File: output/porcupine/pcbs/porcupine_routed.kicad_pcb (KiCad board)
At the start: 2 copper layers, 129.4 x 113.9 mm, 54 parts, among them J1 Jumper, J2 Jumper

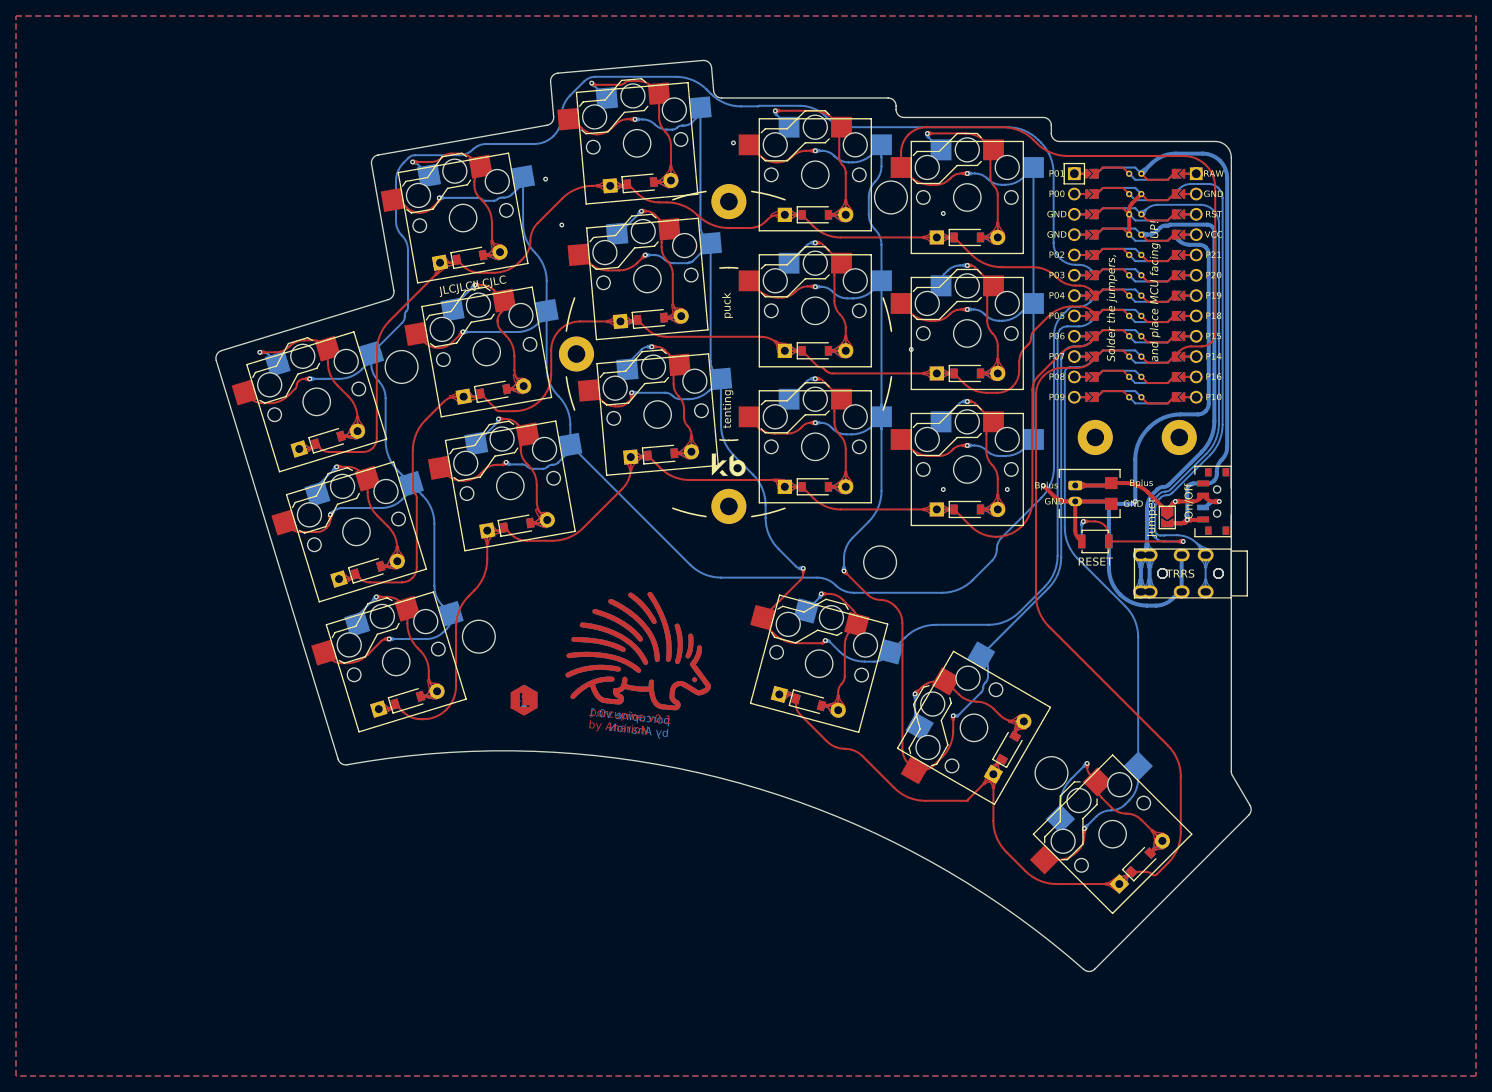
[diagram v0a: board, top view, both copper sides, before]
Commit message: Add new logo
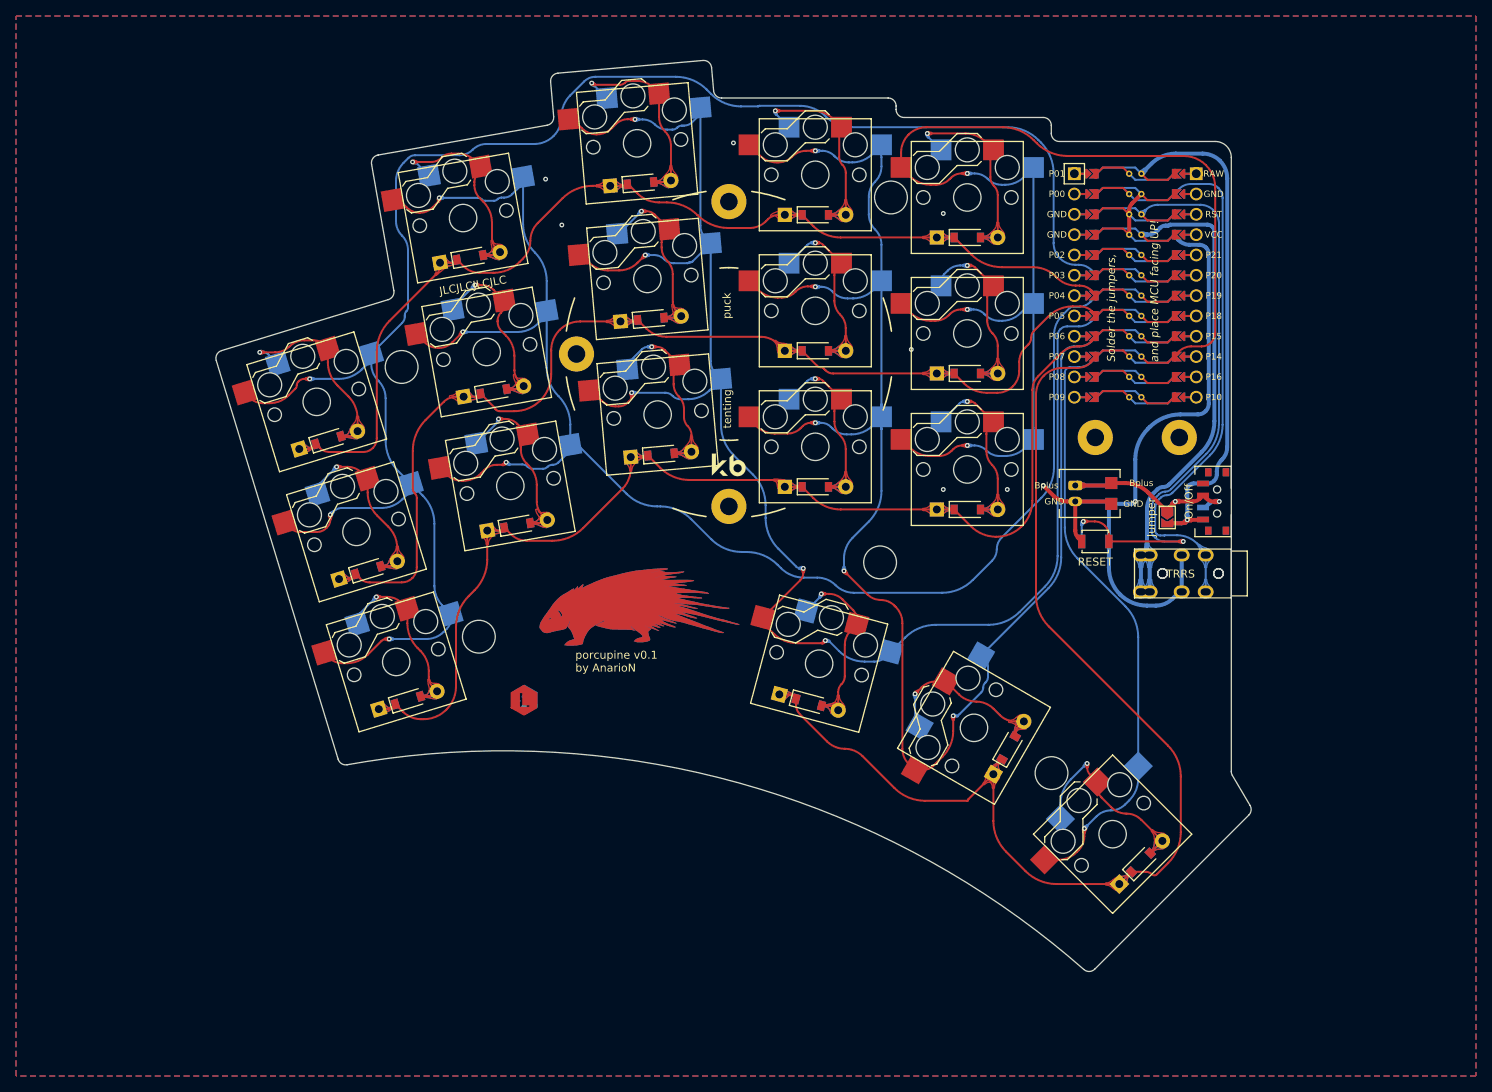
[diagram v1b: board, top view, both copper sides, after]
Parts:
- moved LOGO_B 5.28 mm to (205.4, 143.9), turned to 0 degrees
- moved LOGO_F 5.28 mm to (205.4, 143.9), turned to 0 degrees
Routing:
- net P19: track 192.7 -> 192.0 mm
